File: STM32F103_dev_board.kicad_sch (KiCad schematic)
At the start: 33 parts, among them IC1 TLV70233DBVR, IC2 FT232RNL-REEL, J1 Conn_ARM_JTAG_SWD_20, J2 Conn_01x20_Pin, J3 Conn_01x20_Pin, J4 Conn_02x03_Odd_Even, J6 USB4800-03-A, U1 STM32F103RBTx, Y1 8MHz, Y2 Crystal_GND23

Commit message: Changed 0603 footprints to hand solderable ones
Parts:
- C1, C10, C11, C12, C2, C3, C4, C5, C6: footprint Capacitor_SMD:C_0201_0603Metric -> Capacitor_SMD:C_0603_1608Metric_Pad1.08x0.95mm_HandSolder
- D1, D2: footprint LED_SMD:LED_0201_0603Metric -> LED_SMD:LED_0603_1608Metric_Pad1.05x0.95mm_HandSolder
- R1, R10, R11, R12, R2, R3, R4, R5, R6, R7, R9: footprint Resistor_SMD:R_0201_0603Metric -> Resistor_SMD:R_0603_1608Metric_Pad0.98x0.95mm_HandSolder
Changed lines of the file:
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@@
     (title "STM32F103RBT6 Dev Board")
     (date "2023-09-25")
-    (rev "1.0.1")
+    (rev "1.1.0")
   )
   (junction (at 201.93 35.56) (diameter 0) (color 0 0 0 0)
@@
       (effects (font (size 1.27 1.27)) (justify right))
     )
-    (property "Footprint" "Capacitor_SMD:C_0201_0603Metric" (at 156.5148 80.01 0)
+    (property "Footprint" "Capacitor_SMD:C_0603_1608Metric_Pad1.08x0.95mm_HandSolder" (at 156.5148 80.01 0)
       (effects (font (size 1.27 1.27)) hide)
     )
@@
       (effects (font (size 1.27 1.27)) (justify right))
     )
-    (property "Footprint" "Capacitor_SMD:C_0201_0603Metric" (at 146.3548 59.69 0)
+    (property "Footprint" "Capacitor_SMD:C_0603_1608Metric_Pad1.08x0.95mm_HandSolder" (at 146.3548 59.69 0)
       (effects (font (size 1.27 1.27)) hide)
     )
@@
       (effects (font (size 1.27 1.27)))
     )
-    (property "Footprint" "Capacitor_SMD:C_0201_0603Metric" (at 139.7 54.3052 0)
+    (property "Footprint" "Capacitor_SMD:C_0603_1608Metric_Pad1.08x0.95mm_HandSolder" (at 139.7 54.3052 0)
       (effects (font (size 1.27 1.27)) hide)
     )
@@
       (effects (font (size 1.27 1.27)))
     )
-    (property "Footprint" "Resistor_SMD:R_0201_0603Metric" (at 29.21 42.418 90)
+    (property "Footprint" "Resistor_SMD:R_0603_1608Metric_Pad0.98x0.95mm_HandSolder" (at 29.21 42.418 90)
       (effects (font (size 1.27 1.27)) hide)
     )
@@
       (effects (font (size 1.27 1.27)) (justify right))
     )
-    (property "Footprint" "Capacitor_SMD:C_0201_0603Metric" (at 217.4748 26.67 0)
+    (property "Footprint" "Capacitor_SMD:C_0603_1608Metric_Pad1.08x0.95mm_HandSolder" (at 217.4748 26.67 0)
       (effects (font (size 1.27 1.27)) hide)
     )
@@
       (effects (font (size 1.27 1.27)) (justify right))
     )
-    (property "Footprint" "Resistor_SMD:R_0201_0603Metric" (at 210.058 67.31 90)
+    (property "Footprint" "Resistor_SMD:R_0603_1608Metric_Pad0.98x0.95mm_HandSolder" (at 210.058 67.31 90)
       (effects (font (size 1.27 1.27)) hide)
     )
@@
       (effects (font (size 1.27 1.27)) (justify right))
     )
-    (property "Footprint" "Capacitor_SMD:C_0201_0603Metric" (at 179.3748 24.13 0)
+    (property "Footprint" "Capacitor_SMD:C_0603_1608Metric_Pad1.08x0.95mm_HandSolder" (at 179.3748 24.13 0)
       (effects (font (size 1.27 1.27)) hide)
     )
@@
       (effects (font (size 1.27 1.27)) (justify right))
     )
-    (property "Footprint" "LED_SMD:LED_0201_0603Metric" (at 196.85 55.88 0)
+    (property "Footprint" "LED_SMD:LED_0603_1608Metric_Pad1.05x0.95mm_HandSolder" (at 196.85 55.88 0)
       (effects (font (size 1.27 1.27)) hide)
     )
@@
       (effects (font (size 1.27 1.27)) (justify right))
     )
-    (property "Footprint" "Capacitor_SMD:C_0201_0603Metric" (at 174.2948 80.01 0)
+    (property "Footprint" "Capacitor_SMD:C_0603_1608Metric_Pad1.08x0.95mm_HandSolder" (at 174.2948 80.01 0)
       (effects (font (size 1.27 1.27)) hide)
     )
@@
       (effects (font (size 1.27 1.27)))
     )
-    (property "Footprint" "Capacitor_SMD:C_0201_0603Metric" (at 247.65 23.1648 0)
+    (property "Footprint" "Capacitor_SMD:C_0603_1608Metric_Pad1.08x0.95mm_HandSolder" (at 247.65 23.1648 0)
       (effects (font (size 1.27 1.27)) hide)
     )
@@
       (effects (font (size 1.27 1.27)))
     )
-    (property "Footprint" "Resistor_SMD:R_0201_0603Metric" (at 29.21 43.942 90)
+    (property "Footprint" "Resistor_SMD:R_0603_1608Metric_Pad0.98x0.95mm_HandSolder" (at 29.21 43.942 90)
       (effects (font (size 1.27 1.27)) hide)
     )
@@
       (effects (font (size 1.27 1.27)))
     )
-    (property "Footprint" "Resistor_SMD:R_0201_0603Metric" (at 270.51 62.992 90)
+    (property "Footprint" "Resistor_SMD:R_0603_1608Metric_Pad0.98x0.95mm_HandSolder" (at 270.51 62.992 90)
       (effects (font (size 1.27 1.27)) hide)
     )
@@
       (effects (font (size 1.27 1.27)))
     )
-    (property "Footprint" "Resistor_SMD:R_0201_0603Metric" (at 77.47 33.782 90)
+    (property "Footprint" "Resistor_SMD:R_0603_1608Metric_Pad0.98x0.95mm_HandSolder" (at 77.47 33.782 90)
       (effects (font (size 1.27 1.27)) hide)
     )
@@
       (effects (font (size 1.27 1.27)) (justify right))
     )
-    (property "Footprint" "Resistor_SMD:R_0201_0603Metric" (at 198.628 67.31 90)
+    (property "Footprint" "Resistor_SMD:R_0603_1608Metric_Pad0.98x0.95mm_HandSolder" (at 198.628 67.31 90)
       (effects (font (size 1.27 1.27)) hide)
     )
@@
       (effects (font (size 1.27 1.27)) (justify left))
     )
-    (property "Footprint" "Resistor_SMD:R_0201_0603Metric" (at 179.832 140.97 90)
+    (property "Footprint" "Resistor_SMD:R_0603_1608Metric_Pad0.98x0.95mm_HandSolder" (at 179.832 140.97 90)
       (effects (font (size 1.27 1.27)) hide)
     )
@@
       (effects (font (size 1.27 1.27)) (justify left))
     )
-    (property "Footprint" "Resistor_SMD:R_0201_0603Metric" (at 172.212 140.97 90)
+    (property "Footprint" "Resistor_SMD:R_0603_1608Metric_Pad0.98x0.95mm_HandSolder" (at 172.212 140.97 90)
       (effects (font (size 1.27 1.27)) hide)
     )
@@
       (effects (font (size 1.27 1.27)))
     )
-    (property "Footprint" "Capacitor_SMD:C_0201_0603Metric" (at 38.1 124.1552 0)
+    (property "Footprint" "Capacitor_SMD:C_0603_1608Metric_Pad1.08x0.95mm_HandSolder" (at 38.1 124.1552 0)
       (effects (font (size 1.27 1.27)) hide)
     )
@@
       (effects (font (size 1.27 1.27)))
     )
-    (property "Footprint" "Resistor_SMD:R_0201_0603Metric" (at 29.21 41.402 90)
+    (property "Footprint" "Resistor_SMD:R_0603_1608Metric_Pad0.98x0.95mm_HandSolder" (at 29.21 41.402 90)
       (effects (font (size 1.27 1.27)) hide)
     )
@@
       (effects (font (size 1.27 1.27)) (justify right))
     )
-    (property "Footprint" "LED_SMD:LED_0201_0603Metric" (at 208.28 55.88 0)
+    (property "Footprint" "LED_SMD:LED_0603_1608Metric_Pad1.05x0.95mm_HandSolder" (at 208.28 55.88 0)
       (effects (font (size 1.27 1.27)) hide)
     )
@@
       (effects (font (size 1.27 1.27)))
     )
-    (property "Footprint" "Capacitor_SMD:C_0201_0603Metric" (at 247.65 39.6748 0)
+    (property "Footprint" "Capacitor_SMD:C_0603_1608Metric_Pad1.08x0.95mm_HandSolder" (at 247.65 39.6748 0)
       (effects (font (size 1.27 1.27)) hide)
     )
@@
       (effects (font (size 1.27 1.27)))
     )
-    (property "Footprint" "Resistor_SMD:R_0201_0603Metric" (at 238.76 62.992 90)
+    (property "Footprint" "Resistor_SMD:R_0603_1608Metric_Pad0.98x0.95mm_HandSolder" (at 238.76 62.992 90)
       (effects (font (size 1.27 1.27)) hide)
     )
@@
       (effects (font (size 1.27 1.27)) (justify left))
     )
-    (property "Footprint" "Resistor_SMD:R_0201_0603Metric" (at 187.452 140.97 90)
-      (effects (font (size 1.27 1.27)) hide)
-    )
+    (property "Footprint" "Resistor_SMD:R_0603_1608Metric_Pad0.98x0.95mm_HandSolder" (at 187.452 140.97 90)
+      (effects (font (size 1.27 1.27)) hide)
+    )

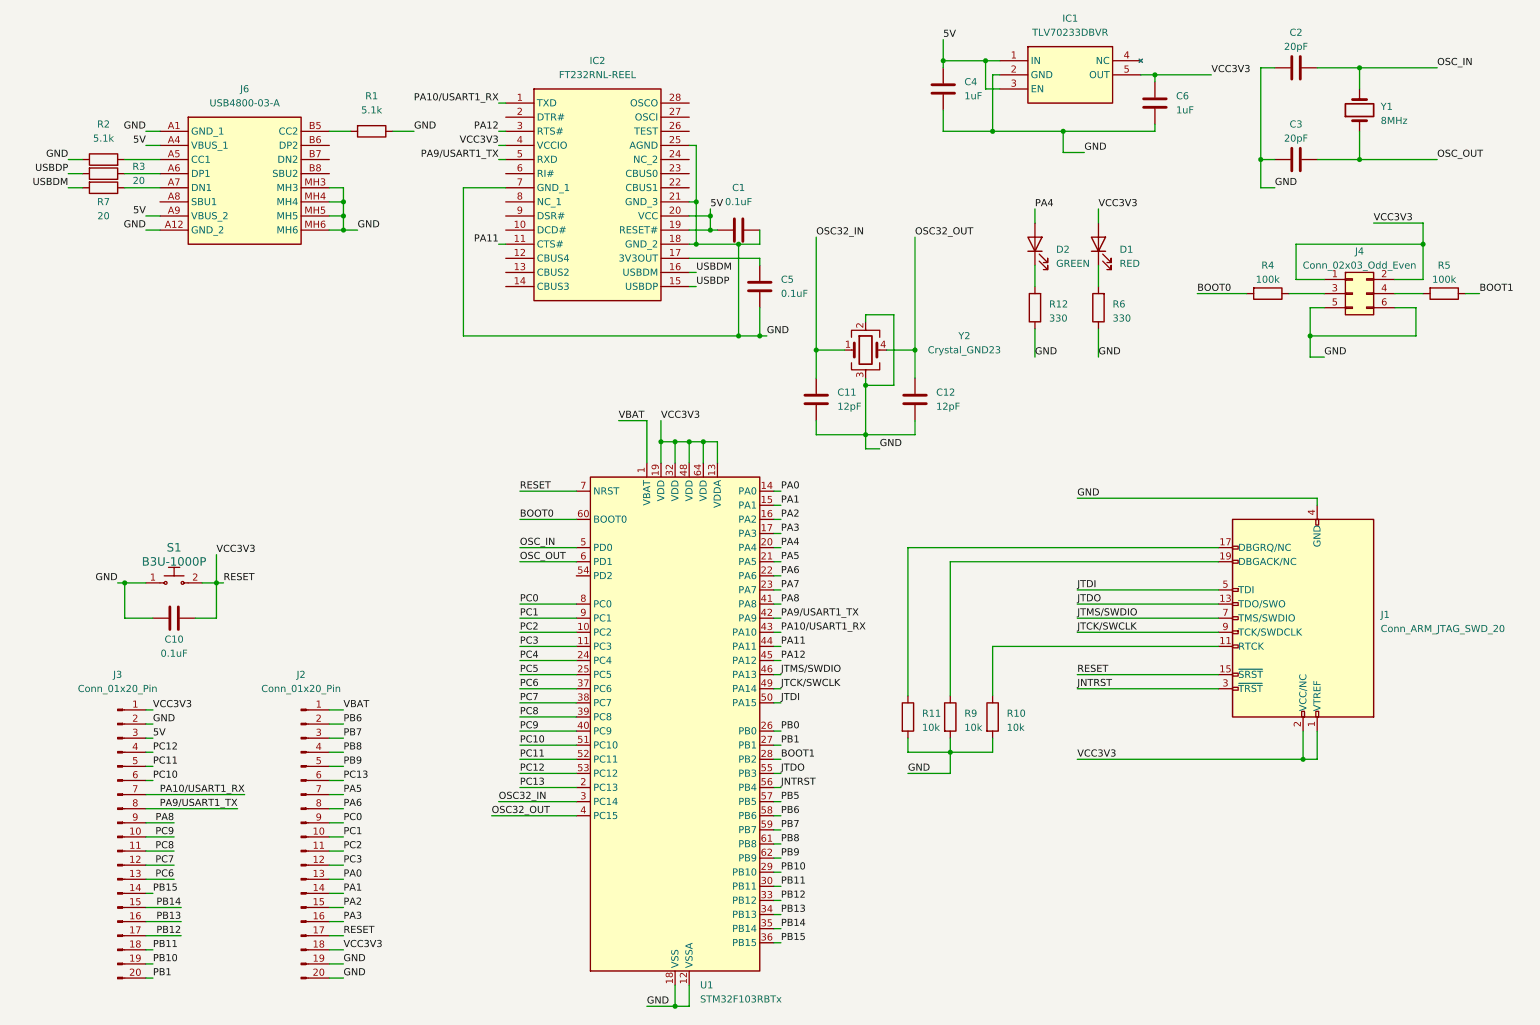
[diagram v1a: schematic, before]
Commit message: Fixed some labels and updated production files
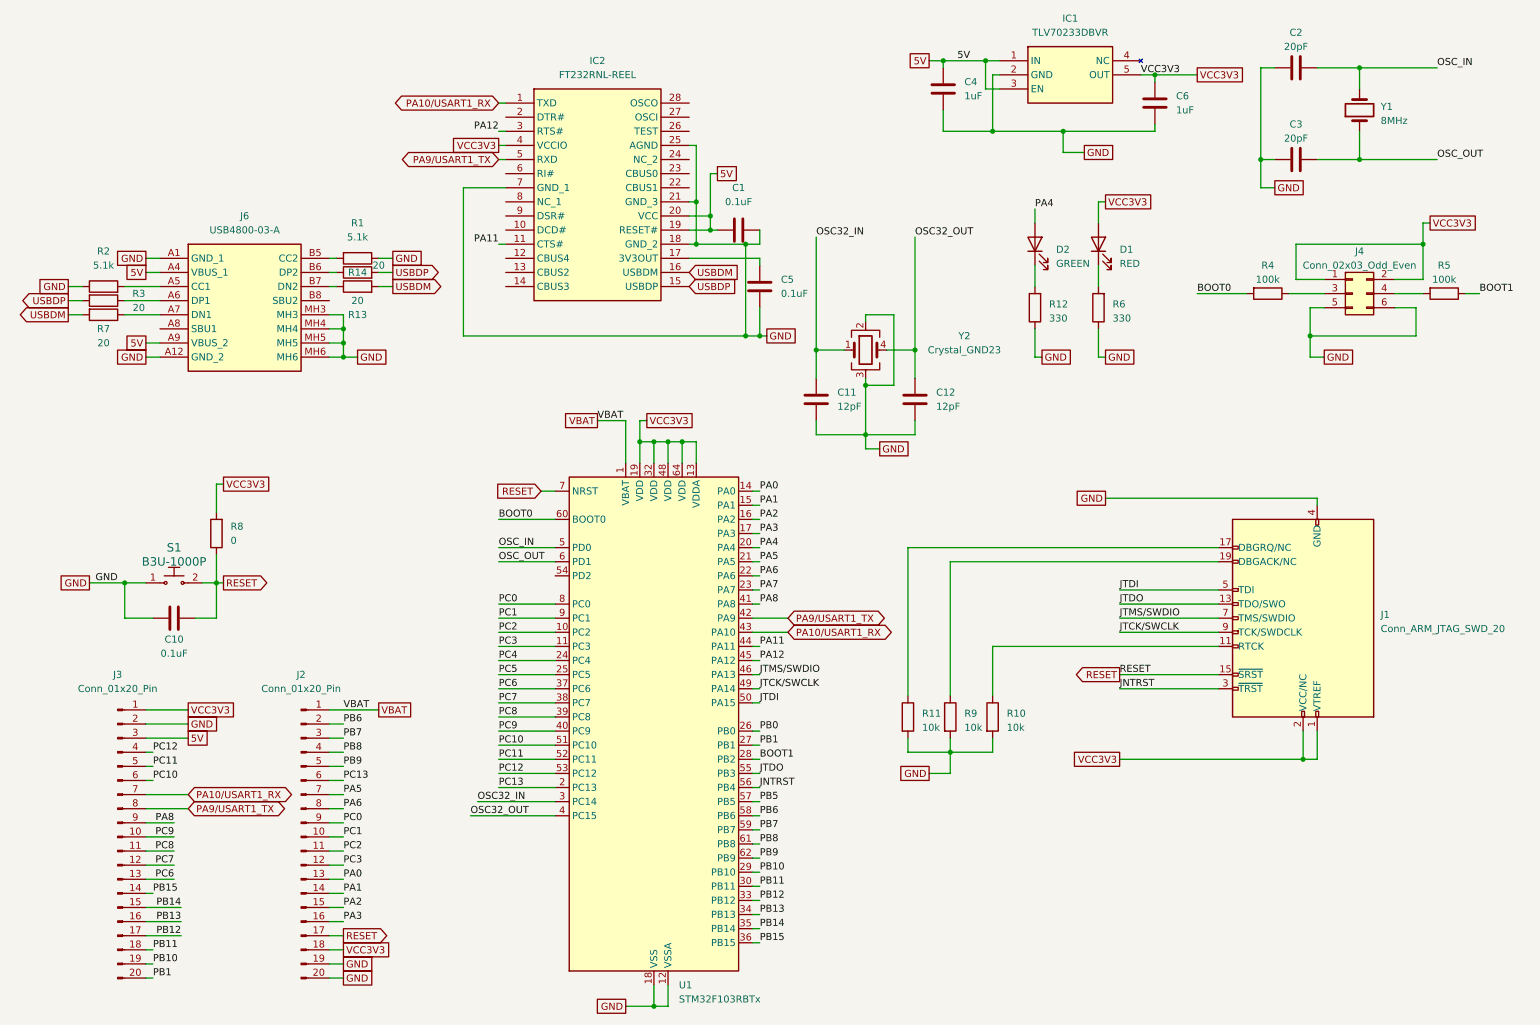
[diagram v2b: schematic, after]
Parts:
- added R13, R14: 20, Resistor_SMD:R_0603_1608Metric_Pad0.98x0.95mm_HandSolder, symbol Device:R
- added R8: 0, Resistor_SMD:R_0603_1608Metric_Pad0.98x0.95mm_HandSolder, symbol Device:R
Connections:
- net RESET: now also R8.1; no longer C6.2, D1.2 (A), IC1.5 (OUT), IC2.4 (VCCIO), J1.1 (VTREF), J1.2 (VCC/NC), J2.18 (Pin_18), J3.1 (Pin_1), J4.1 (Pin_1), J4.2 (Pin_2), U1.13 (VDDA), U1.19 (VDD), U1.32 (VDD), U1.48 (VDD), U1.64 (VDD)
- net USBDM: now also R13.2
- net USBDP: now also R14.2
- net at J6.B6 (DP2): now also R14.1
- net at J6.B7 (DN2): now also R13.1
- new net VCC3V3: C6.2, D1.2 (A), IC1.5 (OUT), IC2.4 (VCCIO), J1.1 (VTREF), J1.2 (VCC/NC), J2.18 (Pin_18), J3.1 (Pin_1), J4.1 (Pin_1), J4.2 (Pin_2), R8.2, U1.13 (VDDA), U1.19 (VDD), U1.32 (VDD), U1.48 (VDD), U1.64 (VDD)
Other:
- moved on the sheet: J6, R1, R2, R3, R7, U1

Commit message: Removed external pull-up resistor in reset switch
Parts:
- removed R8: 0, Resistor_SMD:R_0603_1608Metric_Pad0.98x0.95mm_HandSolder, symbol Device:R
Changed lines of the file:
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@@
     (title "STM32F103RBT6 Dev Board")
     (date "2023-10-13")
-    (rev "1.1.1")
+    (rev "1.1.2")
   )
   (junction (at 201.93 35.56) (diameter 0) (color 0 0 0 0)
@@
     (stroke (width 0) (type default))
   )
-  (wire (pts (xy 49.53 99.06) (xy 49.53 104.14))
-    (stroke (width 0) (type default))
-  )
   (wire (pts (xy 212.09 118.11) (xy 229.87 118.11))
     (stroke (width 0) (type default))
@@
     (stroke (width 0) (type default))
   )
-  (wire (pts (xy 49.53 111.76) (xy 49.53 116.84))
-    (stroke (width 0) (type default))
-  )
   (wire (pts (xy 36.83 144.78) (xy 44.45 144.78))
     (stroke (width 0) (type default))
@@
   )
   (wire (pts (xy 69.85 68.58) (xy 72.39 68.58))
-    (stroke (width 0) (type default))
-  )
-  (wire (pts (xy 50.8 99.06) (xy 49.53 99.06))
     (stroke (width 0) (type default))
   )
@@
     (effects (font (size 1.27 1.27)) (justify left))
     (property "Intersheetrefs" "${INTERSHEET_REFS}" (at 85.0287 139.7 0)
-      (effects (font (size 1.27 1.27)) (justify left) hide)
-    )
-  )
-  (global_label "VCC3V3" (shape passive) (at 50.8 99.06 0) (fields_autoplaced)
-    (effects (font (size 1.27 1.27)) (justify left))
-    (property "Intersheetrefs" "${INTERSHEET_REFS}" (at 59.8101 99.06 0)
       (effects (font (size 1.27 1.27)) (justify left) hide)
     )
@@
         )
       )
-    )
-  )
-  (symbol (lib_id "Device:R") (at 49.53 107.95 180) (unit 1)
-    (in_bom yes) (on_board yes) (dnp no) (fields_autoplaced)
-    (property "Reference" "R8" (at 52.07 106.68 0)
-      (effects (font (size 1.27 1.27)) (justify right))
-    )
-    (property "Value" "0" (at 52.07 109.22 0)
-      (effects (font (size 1.27 1.27)) (justify right))
-    )
-    (property "Footprint" "Resistor_SMD:R_0603_1608Metric_Pad0.98x0.95mm_HandSolder" (at 51.308 107.95 90)
-      (effects (font (size 1.27 1.27)) hide)
-    )
-    (property "Datasheet" "~" (at 49.53 107.95 0)
-      (effects (font (size 1.27 1.27)) hide)
-    )
-    (pin "1")
-    (pin "2")
-    (instances
-      (project "STM32F103_dev_board"
-        (path "/93ed7a92-70c4-4662-9ca1-0ce61928fd3a"
-          (reference "R8") (unit 1)
-        )
-      )
